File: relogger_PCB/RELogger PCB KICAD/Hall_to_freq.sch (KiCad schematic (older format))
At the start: 4 parts, among them P26 JMP_HALL, U6 LM393

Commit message: Schematic uploaded with Arduino Nano, SD Card connector and DS3231 connector
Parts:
- D16: symbol ZENER -> ZENER-RESCUE-RELogger_PCB_v1
- RV1: symbol POT -> POT-RESCUE-RELogger_PCB_v1
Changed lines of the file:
@@
 LIBS:matts_components
 LIBS:linear2
+LIBS:ds3231
+LIBS:micro_sd
 LIBS:RELogger_PCB_v1-cache
 EELAYER 25 0
@@
 Connection ~ 6600 2300
 $Comp
-L POT RV1
+L POT-RESCUE-RELogger_PCB_v1 RV1
 U 1 1 57B16B0C
 P 5550 3350
@@
 $EndComp
 $Comp
-L ZENER D16
+L ZENER-RESCUE-RELogger_PCB_v1 D16
 U 1 1 57B7AFA3
 P 4800 3400

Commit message: Update of schematic
By ML
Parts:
- RV1: value POT -> 100k
- U6: Description (none) -> Op Amp; Manufacturer (none) -> ON Semi; Manufacturer Part No (none) -> LM393NG; Supplier 1 (none) -> RS; Supplier 1 Cost (none) -> 0.25; Supplier 1 Part No (none) -> 463-870
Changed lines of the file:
@@
 LIBS:matts_components
 LIBS:linear2
-LIBS:ds3231
-LIBS:micro_sd
 LIBS:RELogger_PCB_v1-cache
 EELAYER 25 0
@@
 F 1 "LM393" H 6950 3100 50  0000 C CNN
 F 2 "" H 6700 3250 50  0000 C CNN
-F 3 "" H 6700 3250 50  0000 C CNN
+F 3 "http://docs-europe.electrocomponents.com/webdocs/13e4/0900766b813e452a.pdf" H 6700 3250 50  0001 C CNN
+F 4 "~" H 6700 3250 60  0000 C CNN "Notes"
+F 5 "Op Amp" H 6700 3250 60  0001 C CNN "Description"
+F 6 "ON Semi" H 6700 3250 60  0001 C CNN "Manufacturer"
+F 7 "LM393NG" H 6700 3250 60  0001 C CNN "Manufacturer Part No"
+F 8 "RS" H 6700 3250 60  0001 C CNN "Supplier 1"
+F 9 "463-870" H 6700 3250 60  0001 C CNN "Supplier 1 Part No"
+F 10 "0.25" H 6700 3250 60  0001 C CNN "Supplier 1 Cost"
+F 11 "~" H 6700 3250 60  0001 C CNN "Supplier 2"
+F 12 "~" H 6700 3250 60  0001 C CNN "Supplier 2 Part No"
+F 13 "~" H 6700 3250 60  0001 C CNN "Supplier 2 Cost"
 	1    6700 3250
 	1    0    0    -1
@@
 P 5550 3350
 F 0 "RV1" H 5550 3250 50  0000 C CNN
-F 1 "POT" H 5550 3350 50  0000 C CNN
+F 1 "100k" H 5550 3350 50  0000 C CNN
 F 2 "" H 5550 3350 50  0000 C CNN
 F 3 "" H 5550 3350 50  0000 C CNN

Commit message: Schematic update and PCB initial run
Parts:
- D16: footprint (none) -> REInnovationFootprint:TH_Diode_1
- P26: footprint (none) -> REInnovationFootprint:SM_2_SLDR_JMP
- RV1: footprint (none) -> REInnovationFootprint:RV_various_lg_pad
- U6: footprint (none) -> REInnovationFootprint:DIP-8_300_ELL
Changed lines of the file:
@@
 F 0 "U6" H 6850 3400 50  0000 C CNN
 F 1 "LM393" H 6950 3100 50  0000 C CNN
-F 2 "" H 6700 3250 50  0000 C CNN
+F 2 "REInnovationFootprint:DIP-8_300_ELL" H 6700 3250 50  0001 C CNN
 F 3 "http://docs-europe.electrocomponents.com/webdocs/13e4/0900766b813e452a.pdf" H 6700 3250 50  0001 C CNN
 F 4 "~" H 6700 3250 60  0000 C CNN "Notes"
@@
 F 0 "U6" H 6850 4500 50  0000 C CNN
 F 1 "LM393" H 6950 4200 50  0000 C CNN
-F 2 "" H 6700 4350 50  0000 C CNN
+F 2 "REInnovationFootprint:DIP-8_300_ELL" H 6700 4350 50  0001 C CNN
 F 3 "" H 6700 4350 50  0000 C CNN
 F 4 "~" H 6700 4350 60  0001 C CNN "Description"
@@
 F 0 "RV1" H 5550 3250 50  0000 C CNN
 F 1 "100k" H 5550 3350 50  0000 C CNN
-F 2 "" H 5550 3350 50  0000 C CNN
+F 2 "REInnovationFootprint:RV_various_lg_pad" H 5550 3350 50  0001 C CNN
 F 3 "" H 5550 3350 50  0000 C CNN
 	1    5550 3350
@@
 F 0 "P26" H 7550 2950 50  0000 C CNN
 F 1 "JMP_HALL" V 7650 2800 50  0000 C CNN
-F 2 "" H 7550 2800 50  0000 C CNN
+F 2 "REInnovationFootprint:SM_2_SLDR_JMP" H 7550 2800 50  0001 C CNN
 F 3 "" H 7550 2800 50  0000 C CNN
 	1    7550 2800
@@
 F 0 "D16" H 4800 3500 50  0000 C CNN
 F 1 "5V1" H 4800 3300 50  0000 C CNN
-F 2 "" H 4800 3400 50  0000 C CNN
+F 2 "REInnovationFootprint:TH_Diode_1" H 4800 3400 50  0001 C CNN
 F 3 "" H 4800 3400 50  0000 C CNN
 	1    4800 3400

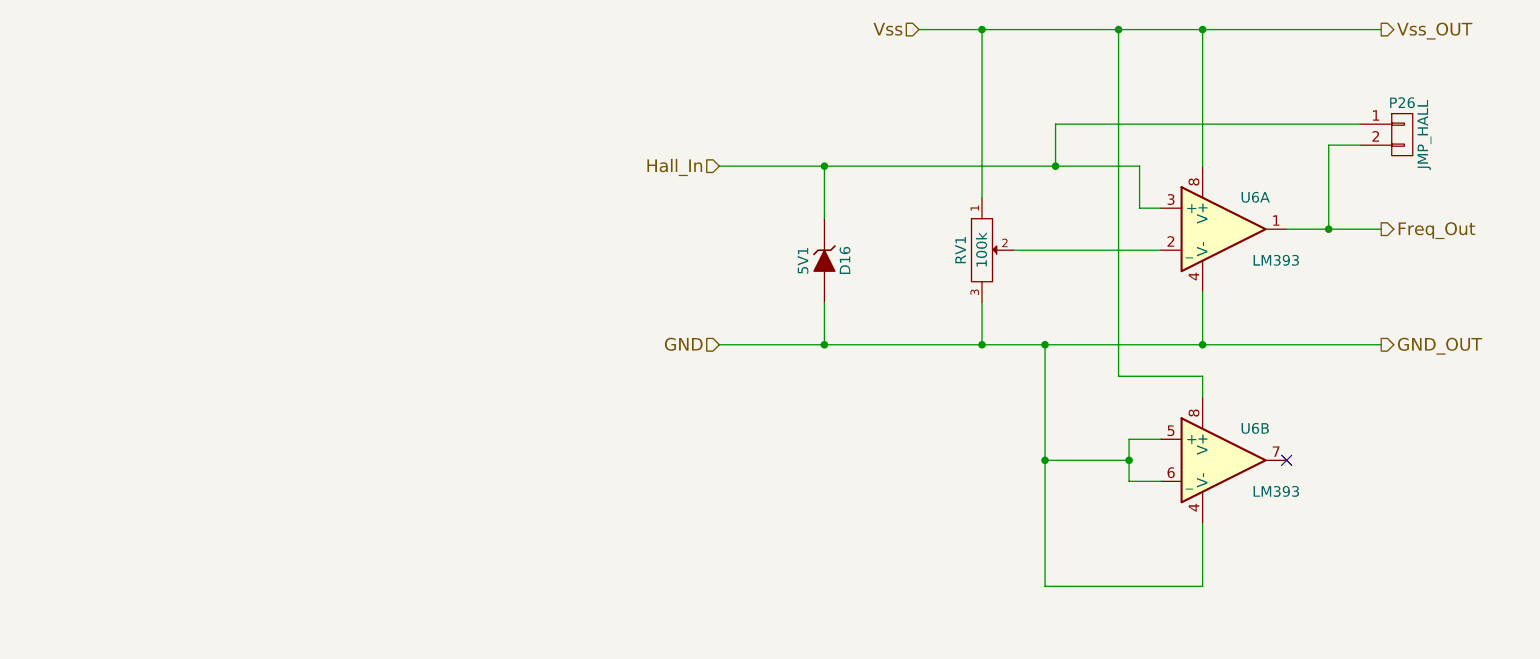
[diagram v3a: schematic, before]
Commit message: Updated schmatic
Debounce switches. Power control for all.
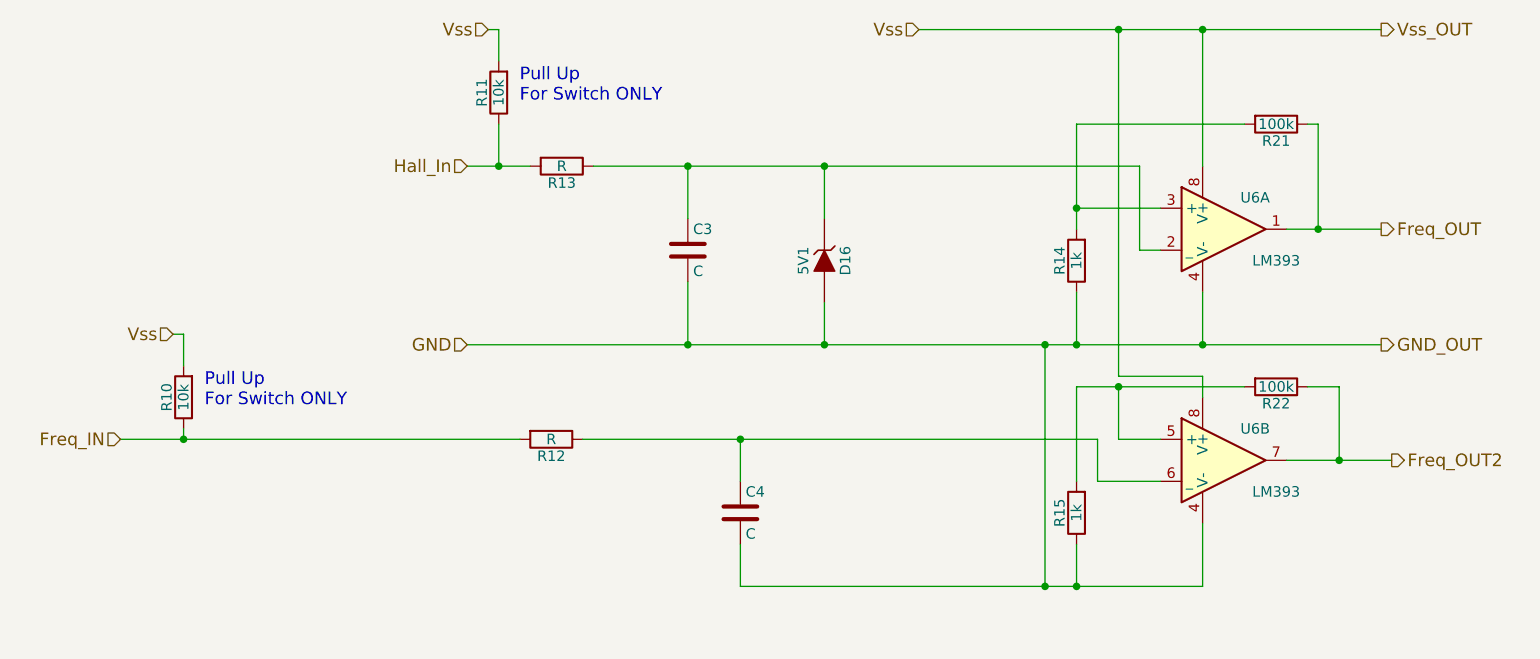
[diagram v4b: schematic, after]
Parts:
- removed P26: JMP_HALL, REInnovationFootprint:SM_2_SLDR_JMP, symbol CONN_01X02
- removed RV1: 100k, REInnovationFootprint:RV_various_lg_pad, symbol POT-RESCUE-RELogger_PCB_v1
- added C3, C4: C, symbol C
- added R10, R11: 10k, symbol R
- added R12, R13: R, symbol R
- added R14, R15: 1k, symbol R
- added R21, R22: 100k, symbol R
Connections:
- net GND: now also C3.2, C4.2, R14.1, R15.1; no longer U6.5 (+), U6.6 (_)
- net Hall_In: now also R11.1, R13.2; no longer D16.1 (K), U6.3 (+)
- net Vss: now also R10.2, R11.2
- net at U6.2 (_): now also D16.1 (K), C3.1, R13.1
- net Freq_OUT2: now reaches U6.7
- net Freq_OUT2: now also R22.1
- net Freq_Out renamed Freq_OUT
- net Freq_OUT: now also R21.1
- new net: R14.2, R21.2, U6.3 (+)
- new net: R15.2, R22.2, U6.5 (+)
- new net: C4.1, R12.1, U6.6 (_)
- new net Freq_IN: R10.1, R12.2
- no-connect marks 1 -> 0
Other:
- note added: "Pull Up\nFor Switch ONLY"

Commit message: Small updates
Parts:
- removed D16: 5V1, REInnovationFootprint:TH_Diode_1, symbol ZENER-RESCUE-RELogger_PCB_v1
- added D?: D, symbol D
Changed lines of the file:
@@
 Wire Wire Line
 	7000 3250 7450 3250
-$Comp
-L ZENER-RESCUE-RELogger_PCB_v1 D16
-U 1 1 57B7AFA3
-P 4800 3400
-F 0 "D16" H 4800 3500 50  0000 C CNN
-F 1 "5V1" H 4800 3300 50  0000 C CNN
-F 2 "REInnovationFootprint:TH_Diode_1" H 4800 3400 50  0001 C CNN
-F 3 "" H 4800 3400 50  0000 C CNN
-	1    4800 3400
-	0    1    1    0
-$EndComp
-Wire Wire Line
-	4800 2950 4800 3200
-Connection ~ 4800 2950
-Wire Wire Line
-	4800 3800 4800 3600
-Connection ~ 4800 3800
 Text HLabel 1450 4250 0    60   Input ~ 0
 Freq_IN
@@
 	6200 4250 6200 4000
 Connection ~ 6200 4000
+$Comp
+L D D?
+U 1 1 595D9167
+P 4650 2650
+F 0 "D?" H 4650 2750 50  0000 C CNN
+F 1 "D" H 4650 2550 50  0000 C CNN
+F 2 "" H 4650 2650 50  0000 C CNN
+F 3 "" H 4650 2650 50  0000 C CNN
+	1    4650 2650
+	0    1    1    0
+$EndComp
 $EndSCHEMATC

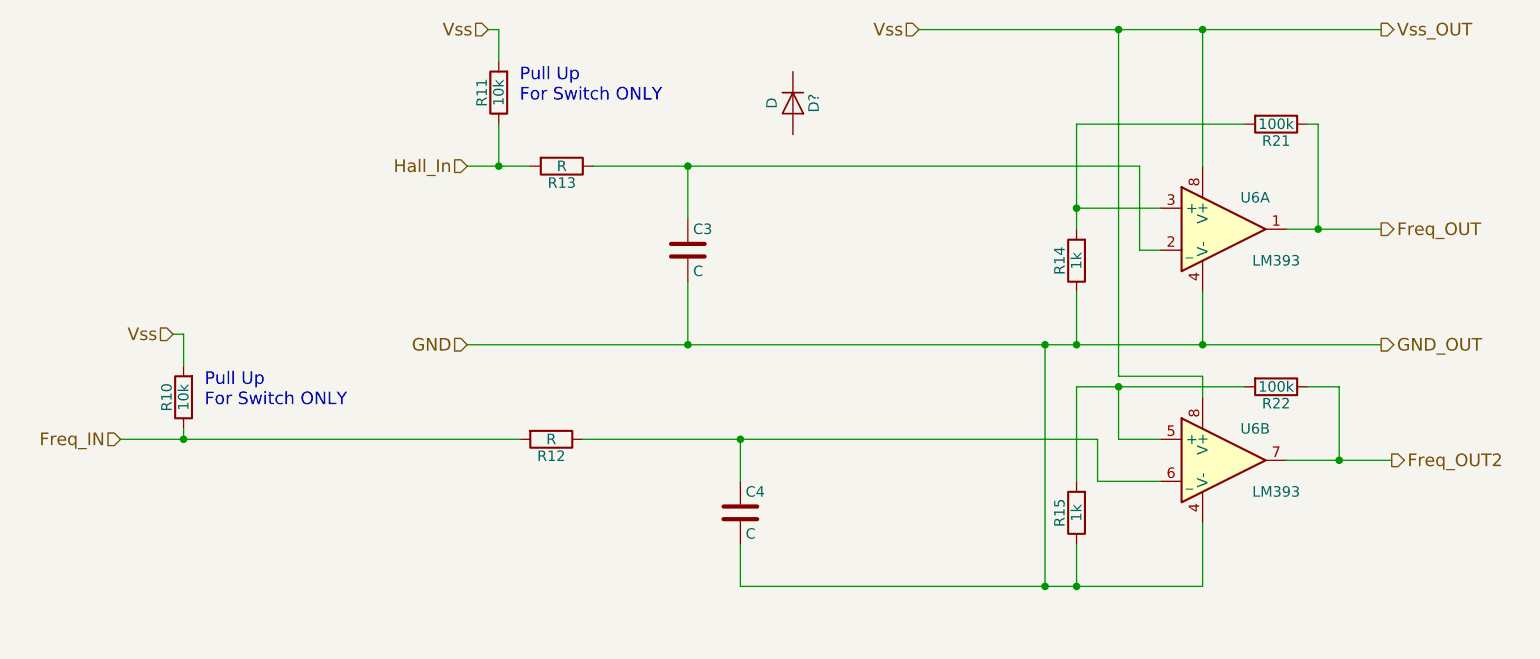
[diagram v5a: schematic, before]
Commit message: Updated new scehmatic.
Still needs Freq conversion circuit. And 3.3V regulator
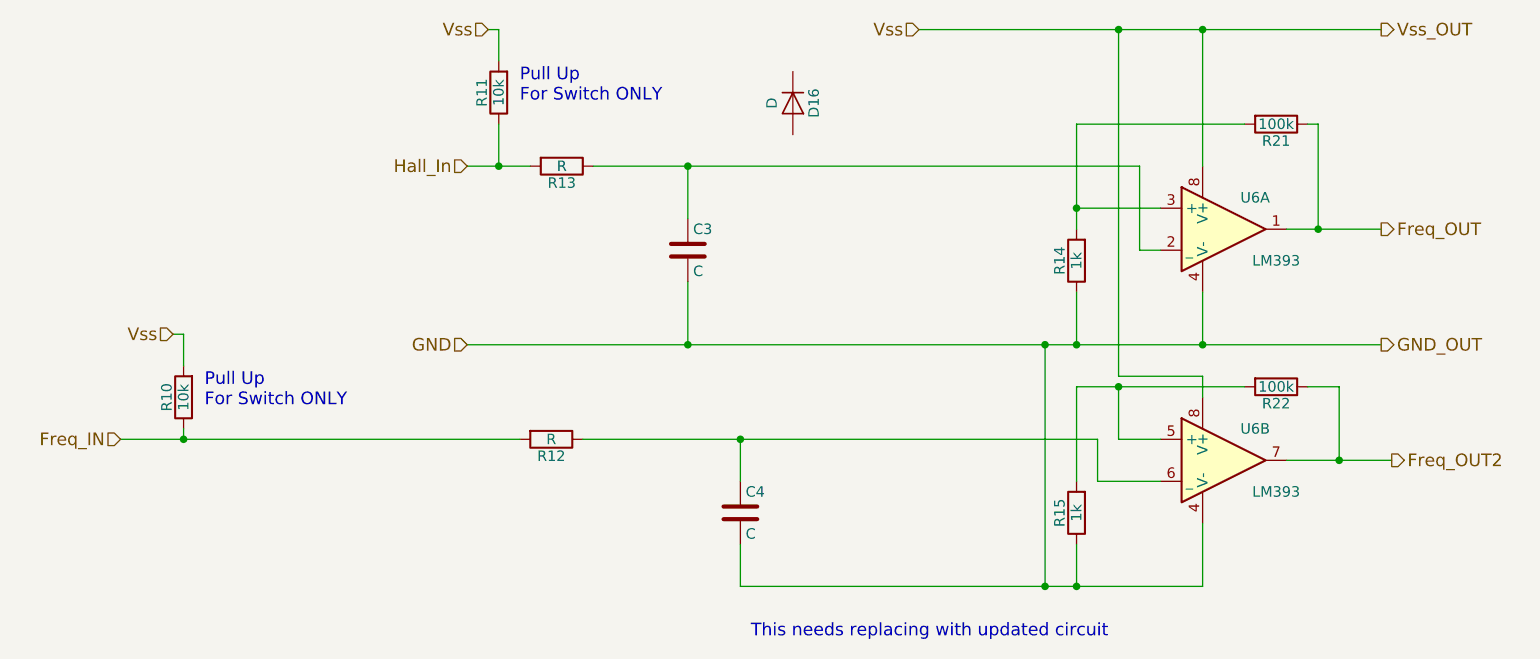
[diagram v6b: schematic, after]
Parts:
- gave numbers to parts that had none: 1
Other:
- note added: "This needs replacing with updated circuit"
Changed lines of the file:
@@
 Connection ~ 6200 4000
 $Comp
-L D D?
+L D D16
 U 1 1 595D9167
 P 4650 2650
-F 0 "D?" H 4650 2750 50  0000 C CNN
+F 0 "D16" H 4650 2750 50  0000 C CNN
 F 1 "D" H 4650 2550 50  0000 C CNN
 F 2 "" H 4650 2650 50  0000 C CNN
@@
 	0    1    1    0
 $EndComp
+Text Notes 4450 5200 0    60   ~ 0
+This needs replacing with updated circuit
 $EndSCHEMATC
